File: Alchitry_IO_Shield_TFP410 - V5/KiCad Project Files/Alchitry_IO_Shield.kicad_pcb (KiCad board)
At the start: 2 copper layers, 65 x 45 mm, 75 parts, among them J0 HDMI_A_1.4, Q1 Q_PMOS_SGD, Q2 Q_PMOS_SGD, Q3 Q_PMOS_SGD, Q4 Q_PMOS_SGD, SW1 SW_DIP_x08, SW2 SW_DIP_x08, SW3 SW_DIP_x08, U0 boardmezzanine_new, U1 TFP410

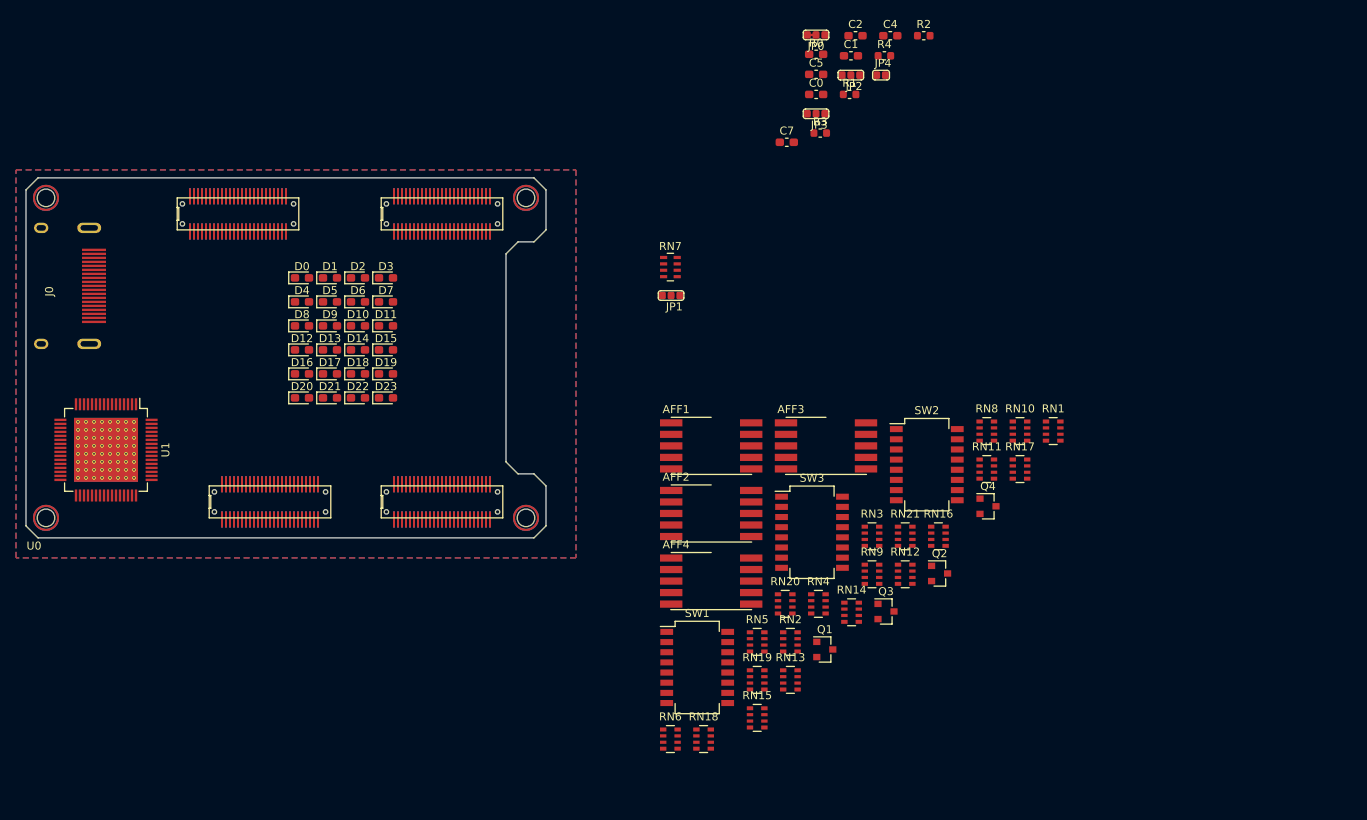
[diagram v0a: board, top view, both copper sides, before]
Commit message: grouped footprints by function
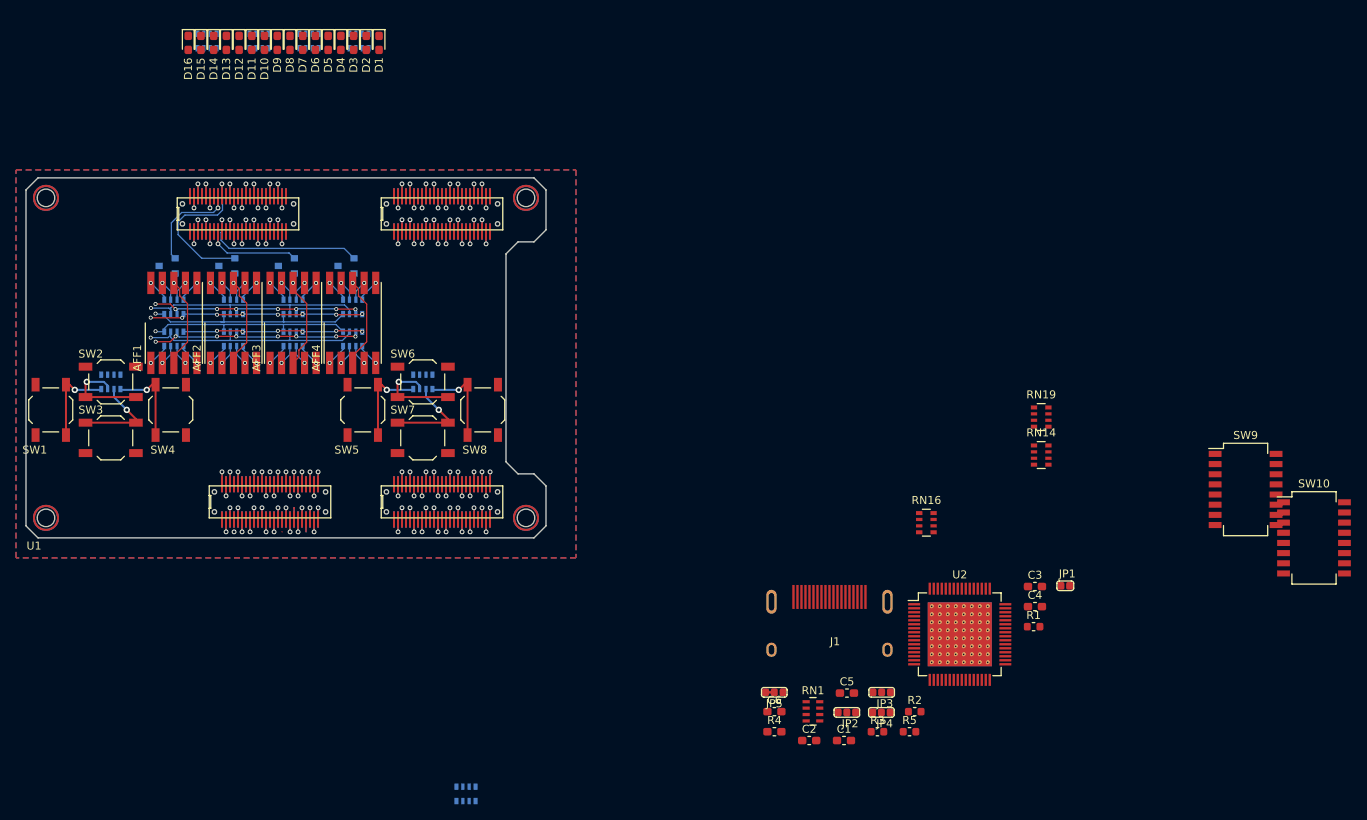
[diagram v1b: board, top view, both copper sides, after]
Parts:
- removed C0, C7: 100nF, Capacitor_SMD:C_0603_1608Metric_Pad1.05x0.95mm_HandSolder
- removed D0, D17, D18, D19, D20, D21, D22, D23: LED, LED_SMD:LED_0603_1608Metric_Pad1.05x0.95mm_HandSolder
- removed J0: HDMI_A_1.4, Custom_Parts:HDMI
- removed JP0: V_Sel, Custom_Parts:jumper_1_2_bridged
- removed R0: 510, Resistor_SMD:R_0603_1608Metric_Pad1.05x0.95mm_HandSolder
- removed RN20, RN21: R_Pack04, Resistor_SMD:R_Array_Convex_4x0603
- removed the U1 at (22.0, 46.0)
- added C3: 100nF, Capacitor_SMD:C_0603_1608Metric_Pad1.05x0.95mm_HandSolder, F.Cu at (138.1, 63.1)
- added C6: 100nF, Capacitor_SMD:C_0603_1608Metric_Pad1.05x0.95mm_HandSolder, F.Cu at (105.5, 78.7)
- added J1: HDMI_A_1.4, Custom_Parts:HDMI, F.Cu at (116.9, 64.4)
- added JP5: V_Sel, Custom_Parts:jumper_1_2_bridged, F.Cu at (105.5, 76.3)
- added R5: 10K, Resistor_SMD:R_0603_1608Metric, F.Cu at (122.4, 81.2)
- added SW10: SW_DIP_x08, Button_Switch_SMD:SW_DIP_SPSTx08_Slide_Copal_CHS-08B_W7.62mm_P1.27mm, F.Cu at (173.0, 57.0)
- added SW4: SWL4, Button_Switch_SMD:SW_SPST_TL3342, F.Cu at (30.1, 41.0)
- added SW5: SWR3, Button_Switch_SMD:SW_SPST_TL3342, F.Cu at (54.1, 41.0)
- added SW6: SWR1, Button_Switch_SMD:SW_SPST_TL3342, F.Cu at (61.6, 37.5)
- added SW7: SWR2, Button_Switch_SMD:SW_SPST_TL3342, F.Cu at (61.6, 44.5)
- added SW8: SWR3, Button_Switch_SMD:SW_SPST_TL3342, F.Cu at (69.1, 41.0)
- added SW9: SW_DIP_x08, Button_Switch_SMD:SW_DIP_SPSTx08_Slide_Copal_CHS-08B_W7.62mm_P1.27mm, F.Cu at (164.4, 51.0)
- added U2: TFP410, Package_QFP:HTQFP-64-1EP_10x10mm_P0.5mm_EP8x8mm_Mask4.4x4.4mm_ThermalVias, F.Cu at (128.7, 69.0)
- AFF1, AFF2, AFF3, AFF4: footprint Display_7Segment:KCSC02-136 -> Display_7Segment:KCSC02-105
- JP1: value DK1 -> DKEN; footprint Custom_Parts:jumper_unbridged -> Custom_Parts:Jumper_2_Pin_Unbridged
- JP3: value DK3 -> DK1
- JP4: value DKEN -> DK3; footprint Custom_Parts:Jumper_2_Pin_Unbridged -> Custom_Parts:jumper_unbridged
- Q1, Q2, Q3, Q4, RN10, RN11, RN12, RN13, RN15, RN17, RN18, RN2, RN3, RN4, RN5, RN6, RN8, RN9: moved to B.Cu
- R1: value 10K -> 33K
- R2: value 10K -> 91K
- R3: value 33K -> 10K
- R4: value 91K -> 510; footprint Resistor_SMD:R_0603_1608Metric -> Resistor_SMD:R_0603_1608Metric_Pad1.05x0.95mm_HandSolder
- RN1: value R_Pack04 -> 10K; footprint Resistor_SMD:R_Array_Convex_4x0603 -> Resistor_SMD:R_Array_Concave_4x0603
- RN7: value 10K -> R_Pack04; footprint Resistor_SMD:R_Array_Concave_4x0603 -> Resistor_SMD:R_Array_Convex_4x0603; moved to B.Cu
- SW1: value SW_DIP_x08 -> SWL3; footprint Button_Switch_SMD:SW_DIP_SPSTx08_Slide_Copal_CHS-08B_W7.62mm_P1.27mm -> Button_Switch_SMD:SW_SPST_TL3342
- SW2: value SW_DIP_x08 -> SWL1; footprint Button_Switch_SMD:SW_DIP_SPSTx08_Slide_Copal_CHS-08B_W7.62mm_P1.27mm -> Button_Switch_SMD:SW_SPST_TL3342
- SW3: value SW_DIP_x08 -> SWL2; footprint Button_Switch_SMD:SW_DIP_SPSTx08_Slide_Copal_CHS-08B_W7.62mm_P1.27mm -> Button_Switch_SMD:SW_SPST_TL3342
- moved RN15 109.0 mm to (34.6, -5.11), turned to 90 degrees
- moved RN12 104.7 mm to (41.1, -5.11), turned to 90 degrees
- moved SW2 102.5 mm to (22.6, 37.5), turned to 180 degrees
- moved Q2 97.0 mm to (37.1, 23.0), turned to 180 degrees
- moved RN9 96.9 mm to (47.4, -5.11), turned to 90 degrees
- moved Q1 95.2 mm to (29.6, 23.0), turned to 180 degrees
- moved RN4 92.7 mm to (22.6, 37.5), turned to 90 degrees
- moved RN3 91.9 mm to (30.5, 28.1), turned to 90 degrees
- moved RN10 91.6 mm to (45.4, 32.1), turned to -90 degrees
- moved RN5 90.1 mm to (53.6, -5.11), turned to 90 degrees
- moved RN11 89.1 mm to (45.4, 28.1), turned to 90 degrees
- moved SW3 88.4 mm to (22.6, 44.5)
- moved C2 88.3 mm to (109.9, 82.3)
- moved SW1 87.0 mm to (15.1, 41.0), turned to -90 degrees
- moved Q3 86.5 mm to (44.5, 23.0), turned to 180 degrees
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- renumbered U0 to U1
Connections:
- net /LED17 renamed Net-(U1-PadAB_20)
- net /LED18 renamed Net-(U1-PadAB_18)
- net /LED19 renamed Net-(U1-PadAB_17)
- net /LED20 renamed Net-(U1-PadAB_15)
- net /LED21 renamed Net-(U1-PadAB_14)
- net /LED22 renamed Net-(U1-PadAB_12)
- net /LED23 renamed Net-(U1-PadAB_11)
- D1 pad 2: /LED1 -> /LED0
- D10 pad 2: /LED10 -> /LED9
- D11 pad 2: /LED11 -> /LED10
- D12 pad 2: /LED12 -> /LED11
- D13 pad 2: /LED13 -> /LED12
- D14 pad 2: /LED14 -> /LED13
- D15 pad 2: /LED15 -> /LED14
- D16 pad 2: /LED16 -> /LED15
- D2 pad 2: /LED2 -> /LED1
- D3 pad 2: /LED3 -> /LED2
- D4 pad 2: /LED4 -> /LED3
- D5 pad 2: /LED5 -> /LED4
- D6 pad 2: /LED6 -> /LED5
- D7 pad 2: /LED7 -> /LED6
- D8 pad 2: /LED8 -> /LED7
- D9 pad 2: /LED9 -> /LED8
- JP1 pad 1: +3V3 -> GNDREF
- JP1 pad 2: /HDMI/DK1 -> Net-(JP1-Pad2)
- JP3 pad 2: /HDMI/DK3 -> /HDMI/DK1
- JP4 pad 1: GNDREF -> +3V3
- JP4 pad 2: Net-(JP4-Pad2) -> /HDMI/DK3
- R1 pad 1: /HDMI/ISEL -> Net-(R1-Pad1)
- R1 pad 2: GNDREF -> +3V3
- R2 pad 1: Net-(R2-Pad1) -> Net-(R1-Pad1)
- R3 pad 2: +3V3 -> GNDREF
- R4 pad 1: Net-(R3-Pad1) -> +3V3
- R4 pad 2: GNDREF -> Net-(R4-Pad2)
- RN1 pad 1: GNDREF -> +3V3
- RN1 pad 2: GNDREF -> +3V3
- RN1 pad 3: GNDREF -> +3V3
- RN1 pad 4: GNDREF -> +3V3
- RN1 pad 5: Net-(D3-Pad1) -> Net-(RN1-Pad5)
- RN1 pad 6: Net-(D2-Pad1) -> Net-(RN1-Pad6)
- RN1 pad 7: Net-(D1-Pad1) -> Net-(JP1-Pad2)
- RN10 pad 1: +3V3 -> /C4
- RN10 pad 2: +3V3 -> /C3
- RN10 pad 3: +3V3 -> /C2
- RN10 pad 4: +3V3 -> /DP
- RN10 pad 5: Net-(RN10-Pad5) -> Net-(AFF3-Pad5)
- RN10 pad 6: Net-(RN10-Pad6) -> Net-(AFF3-Pad4)
- RN10 pad 7: Net-(RN10-Pad7) -> Net-(AFF3-Pad2)
- RN10 pad 8: Net-(RN10-Pad8) -> Net-(AFF3-Pad1)
- RN11 pad 1: +3V3 -> /C1
- RN11 pad 2: +3V3 -> /C0
- RN11 pad 3: +3V3 -> /C5
- RN11 pad 4: +3V3 -> /C6
- RN11 pad 5: Net-(RN11-Pad5) -> Net-(AFF3-Pad10)
- RN11 pad 6: Net-(RN11-Pad6) -> Net-(AFF3-Pad9)
- RN11 pad 7: Net-(RN11-Pad7) -> Net-(AFF3-Pad7)
- RN11 pad 8: Net-(RN11-Pad8) -> Net-(AFF3-Pad6)
- RN12 pad 1: +3V3 -> GNDREF
- RN12 pad 2: +3V3 -> GNDREF
- RN12 pad 3: +3V3 -> GNDREF
- RN12 pad 4: +3V3 -> GNDREF
- RN12 pad 5: Net-(RN12-Pad5) -> Net-(D12-Pad1)
- RN12 pad 6: Net-(RN12-Pad6) -> Net-(D11-Pad1)
- RN12 pad 7: Net-(RN12-Pad7) -> Net-(D10-Pad1)
- RN12 pad 8: Net-(RN12-Pad8) -> Net-(D9-Pad1)
- RN13 pad 1: +3V3 -> GNDREF
- RN13 pad 2: +3V3 -> GNDREF
- RN13 pad 3: +3V3 -> GNDREF
- RN13 pad 4: +3V3 -> GNDREF
- RN13 pad 5: Net-(RN13-Pad5) -> /DIP3
- RN13 pad 6: Net-(RN13-Pad6) -> /DIP2
- RN13 pad 7: Net-(RN13-Pad7) -> /DIP1
- RN13 pad 8: Net-(RN13-Pad8) -> /DIP0
- RN14 pad 1: /C0 -> GNDREF
- RN14 pad 2: /C1 -> GNDREF
- RN14 pad 3: /C2 -> GNDREF
- RN14 pad 4: /C3 -> GNDREF
- RN14 pad 5: Net-(AFF1-Pad2) -> /DIP7
- RN14 pad 6: Net-(AFF1-Pad4) -> /DIP6
- RN14 pad 7: Net-(AFF1-Pad6) -> /DIP5
- RN14 pad 8: Net-(AFF1-Pad7) -> /DIP4
- RN15 pad 1: /C0 -> GNDREF
- RN15 pad 2: /C1 -> GNDREF
- RN15 pad 3: /C2 -> GNDREF
- RN15 pad 4: /C3 -> GNDREF
- RN15 pad 5: Net-(AFF2-Pad2) -> Net-(D16-Pad1)
- RN15 pad 6: Net-(AFF2-Pad4) -> Net-(D15-Pad1)
- RN15 pad 7: Net-(AFF2-Pad6) -> Net-(D14-Pad1)
- RN15 pad 8: Net-(AFF2-Pad7) -> Net-(D13-Pad1)
- RN16 pad 1: /C4 -> GNDREF
- RN16 pad 2: /C5 -> GNDREF
- RN16 pad 3: /C6 -> GNDREF
- RN16 pad 4: /DP -> GNDREF
- RN16 pad 5: Net-(AFF1-Pad5) -> /DIP11
- RN16 pad 6: Net-(AFF1-Pad10) -> /DIP10
- RN16 pad 7: Net-(AFF1-Pad9) -> /DIP9
- RN16 pad 8: Net-(AFF1-Pad1) -> /DIP8
- RN17 pad 2: /C5 -> /C3
- RN17 pad 3: /C6 -> /C2
- RN17 pad 5: Net-(AFF2-Pad5) -> Net-(AFF4-Pad5)
- RN17 pad 6: Net-(AFF2-Pad10) -> Net-(AFF4-Pad4)
- RN17 pad 7: Net-(AFF2-Pad9) -> Net-(AFF4-Pad2)
- RN17 pad 8: Net-(AFF2-Pad1) -> Net-(AFF4-Pad1)
- RN18 pad 1: /C0 -> /C1
- RN18 pad 2: /C1 -> /C0
- RN18 pad 3: /C2 -> /C5
- RN18 pad 4: /C3 -> /C6
- RN18 pad 5: Net-(AFF3-Pad2) -> Net-(AFF4-Pad10)
- RN18 pad 6: Net-(AFF3-Pad4) -> Net-(AFF4-Pad9)
- RN18 pad 7: Net-(AFF3-Pad6) -> Net-(AFF4-Pad7)
- RN18 pad 8: Net-(AFF3-Pad7) -> Net-(AFF4-Pad6)
- RN19 pad 1: /C0 -> GNDREF
- RN19 pad 2: /C1 -> GNDREF
- RN19 pad 3: /C2 -> GNDREF
- RN19 pad 4: /C3 -> GNDREF
- RN19 pad 5: Net-(AFF4-Pad2) -> /DIP15
- RN19 pad 6: Net-(AFF4-Pad4) -> /DIP14
- RN19 pad 7: Net-(AFF4-Pad6) -> /DIP13
- RN19 pad 8: Net-(AFF4-Pad7) -> /DIP12
- RN2 pad 1: GNDREF -> /C4
- RN2 pad 2: GNDREF -> /C3
- RN2 pad 3: GNDREF -> /C2
- RN2 pad 4: GNDREF -> /DP
- RN2 pad 5: Net-(D7-Pad1) -> Net-(AFF1-Pad5)
- RN2 pad 6: Net-(D6-Pad1) -> Net-(AFF1-Pad4)
- RN2 pad 7: Net-(D5-Pad1) -> Net-(AFF1-Pad2)
- RN2 pad 8: Net-(D4-Pad1) -> Net-(AFF1-Pad1)
- RN3 pad 1: GNDREF -> /C1
- RN3 pad 2: GNDREF -> /C0
- RN3 pad 3: GNDREF -> /C5
- RN3 pad 4: GNDREF -> /C6
- RN3 pad 5: Net-(D11-Pad1) -> Net-(AFF1-Pad10)
- RN3 pad 6: Net-(D10-Pad1) -> Net-(AFF1-Pad9)
- RN3 pad 7: Net-(D9-Pad1) -> Net-(AFF1-Pad7)
- RN3 pad 8: Net-(D8-Pad1) -> Net-(AFF1-Pad6)
- RN4 pad 1: GNDREF -> /SWL4
- RN4 pad 2: GNDREF -> /SWL2
- RN4 pad 3: GNDREF -> /SWL1
- RN4 pad 4: GNDREF -> /SWL3
- RN4 pad 5: Net-(D15-Pad1) -> GNDREF
- RN4 pad 6: Net-(D14-Pad1) -> GNDREF
- RN4 pad 7: Net-(D13-Pad1) -> GNDREF
- RN4 pad 8: Net-(D12-Pad1) -> GNDREF
- RN5 pad 5: Net-(D19-Pad1) -> Net-(D4-Pad1)
- RN5 pad 6: Net-(D18-Pad1) -> Net-(D3-Pad1)
- RN5 pad 7: Net-(D17-Pad1) -> Net-(D2-Pad1)
- RN5 pad 8: Net-(D16-Pad1) -> Net-(D1-Pad1)
- RN6 pad 1: GNDREF -> /C4
- RN6 pad 2: GNDREF -> /C3
- RN6 pad 3: GNDREF -> /C2
- RN6 pad 4: GNDREF -> /DP
- RN6 pad 5: Net-(D23-Pad1) -> Net-(AFF2-Pad5)
- RN6 pad 6: Net-(D22-Pad1) -> Net-(AFF2-Pad4)
- RN6 pad 7: Net-(D21-Pad1) -> Net-(AFF2-Pad2)
- RN6 pad 8: Net-(D20-Pad1) -> Net-(AFF2-Pad1)
- RN7 pad 1: +3V3 -> /C1
- RN7 pad 2: +3V3 -> /C0
- RN7 pad 3: +3V3 -> /C5
- RN7 pad 4: +3V3 -> /C6
- RN7 pad 5: Net-(RN7-Pad5) -> Net-(AFF2-Pad10)
- RN7 pad 6: Net-(RN7-Pad6) -> Net-(AFF2-Pad9)
- RN7 pad 7: Net-(JP4-Pad2) -> Net-(AFF2-Pad7)
- RN7 pad 8: Net-(RN7-Pad8) -> Net-(AFF2-Pad6)
- RN8 pad 1: +3V3 -> /SWR4
- RN8 pad 2: +3V3 -> /SWR2
- RN8 pad 3: +3V3 -> /SWR1
- RN8 pad 4: +3V3 -> /SWR3
- RN8 pad 5: Net-(RN8-Pad5) -> GNDREF
- RN8 pad 6: Net-(RN8-Pad6) -> GNDREF
- RN8 pad 7: Net-(RN8-Pad7) -> GNDREF
- RN8 pad 8: Net-(RN8-Pad8) -> GNDREF
- RN9 pad 1: +3V3 -> GNDREF
- RN9 pad 2: +3V3 -> GNDREF
- RN9 pad 3: +3V3 -> GNDREF
- RN9 pad 4: +3V3 -> GNDREF
- RN9 pad 5: Net-(RN9-Pad5) -> Net-(D8-Pad1)
- RN9 pad 6: Net-(RN9-Pad6) -> Net-(D7-Pad1)
- RN9 pad 7: Net-(RN9-Pad7) -> Net-(D6-Pad1)
- RN9 pad 8: Net-(RN9-Pad8) -> Net-(D5-Pad1)
- SW1 pad 1: /DIP7 -> /SWL3
- SW1 pad 2: /DIP6 -> +3V3
- SW2 pad 1: /DIP15 -> /SWL1
- SW2 pad 2: /DIP14 -> +3V3
- SW3 pad 1: /DIP23 -> /SWL2
- SW3 pad 2: /DIP22 -> +3V3
- U1 pad AB_21: /LED16 -> Net-(U1-PadAB_21)
- U1 pad AB_30: /DIP16 -> Net-(U1-PadAB_30)
- U1 pad AB_31: /DIP17 -> Net-(U1-PadAB_31)
- U1 pad AB_33: /DIP18 -> Net-(U1-PadAB_33)
- U1 pad AB_34: /DIP19 -> Net-(U1-PadAB_34)
- U1 pad AB_36: /DIP20 -> Net-(U1-PadAB_36)
- U1 pad AB_37: /DIP21 -> Net-(U1-PadAB_37)
- U1 pad AB_39: /DIP22 -> Net-(U1-PadAB_39)
- U1 pad AB_40: /DIP23 -> Net-(U1-PadAB_40)
- U1 pad AT_21: /LED16 -> Net-(U1-PadAB_21)
- U1 pad AT_30: /DIP16 -> Net-(U1-PadAB_30)
- U1 pad AT_31: /DIP17 -> Net-(U1-PadAB_31)
- U1 pad AT_33: /DIP18 -> Net-(U1-PadAB_33)
- U1 pad AT_34: /DIP19 -> Net-(U1-PadAB_34)
- U1 pad AT_36: /DIP20 -> Net-(U1-PadAB_36)
- U1 pad AT_37: /DIP21 -> Net-(U1-PadAB_37)
- U1 pad AT_39: /DIP22 -> Net-(U1-PadAB_39)
- U1 pad AT_40: /DIP23 -> Net-(U1-PadAB_40)
- U1 pad BB_1: Net-(U0-PadBB_1) -> +5V
- U1 pad BB_23: /BTN2 -> /SWL3
- U1 pad BB_24: /BTN3 -> /SWL4
- U1 pad BB_27: /BTN1 -> /SWL2
- U1 pad BB_28: /BTN0 -> /SWL1
- U1 pad BB_50: Net-(U0-PadBB_50) -> +5V
- U1 pad BT_1: Net-(U0-PadBB_1) -> +5V
- U1 pad BT_23: /BTN2 -> /SWL3
- U1 pad BT_24: /BTN3 -> /SWL4
- U1 pad BT_27: /BTN1 -> /SWL2
- U1 pad BT_28: /BTN0 -> /SWL1
- U1 pad BT_50: Net-(U0-PadBB_50) -> +5V
- U1 pad CB_1: Net-(U0-PadCB_1) -> +5V
- U1 pad CB_45: Net-(U0-PadCB_45) -> /SWR4
- U1 pad CB_46: /BTN6 -> /SWR3
- U1 pad CB_48: /BTN5 -> /SWR2
- U1 pad CB_49: /BTN4 -> /SWR1
- U1 pad CB_50: Net-(U0-PadCB_50) -> +5V
- U1 pad CT_1: Net-(U0-PadCB_1) -> +5V
- U1 pad CT_45: Net-(U0-PadCB_45) -> /SWR4
- U1 pad CT_46: /BTN6 -> /SWR3
- U1 pad CT_48: /BTN5 -> /SWR2
- U1 pad CT_49: /BTN4 -> /SWR1
- U1 pad CT_50: Net-(U0-PadCB_50) -> +5V
- U1 pad DB_1: Net-(U0-PadDB_1) -> +5V
- U1 pad DB_50: Net-(U0-PadDB_50) -> +5V
- U1 pad DT_1: Net-(U0-PadDB_1) -> +5V
- U1 pad DT_50: Net-(U0-PadDB_50) -> +5V
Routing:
- net /C5: track 0.00 -> 32.5 mm, vias 0 -> 2
- net /C3: track 0.00 -> 32.2 mm, vias 0 -> 2
- net /C0: track 0.00 -> 31.2 mm, vias 0 -> 9
- net /C2: track 0.00 -> 31.1 mm, vias 0 -> 9
- net /C1: track 0.00 -> 29.9 mm, vias 0 -> 9
- net /C6: track 0.00 -> 29.7 mm, vias 0 -> 2
- net /C4: track 0.00 -> 29.2 mm, vias 0 -> 2
- net /DP: track 0.00 -> 25.6 mm, vias 0 -> 7
- net /AN3: track 0.00 -> 21.6 mm, vias 0 -> 1
- net /AN1: track 0.00 -> 20.8 mm, vias 0 -> 1
- net /SWL2: track 0.00 -> 14.6 mm, vias 0 -> 2
- net /SWR2: track 0.00 -> 14.6 mm, vias 0 -> 2
- net /SWL1: track 0.00 -> 14.4 mm, vias 0 -> 2
- net /SWR1: track 0.00 -> 14.4 mm, vias 0 -> 2
- net /AN0: track 0.00 -> 14.2 mm, vias 0 -> 1
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
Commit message: minor changes
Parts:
- moved RN8 39.2 mm to (22.4, 37.6)
- moved SW5 39.2 mm to (14.9, 41.1)
- moved SW6 39.2 mm to (22.4, 37.6)
- moved SW7 39.2 mm to (22.4, 44.6)
- moved SW8 39.2 mm to (29.9, 41.1)
- moved SW4 38.5 mm to (68.6, 41.1)
- moved RN4 38.5 mm to (61.1, 37.6)
- moved SW1 38.5 mm to (53.6, 41.1)
- moved SW2 38.5 mm to (61.1, 37.6)
- moved SW3 38.5 mm to (61.1, 44.6)
- moved D1 33.2 mm to (70.2, 25.2)
- moved D2 33.2 mm to (68.6, 25.2)
- moved D6 33.2 mm to (62.2, 25.2)
- moved D8 33.2 mm to (59.0, 25.2)
- moved RN5 33.2 mm to (67.7, 25.0)
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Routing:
- net /SWL1: track 14.4 -> 60.1 mm
- net /SWL2: track 14.6 -> 56.2 mm
- net /SWL3: track 13.9 -> 48.1 mm
- net +3V3: track 8.96 -> 42.8 mm
- net /SWR3: track 13.9 -> 37.1 mm, vias 2 -> 3
- net /SWL4: track 13.9 -> 34.9 mm
- net /AN3: track 21.6 -> 2.66 mm
- net /SWR1: track 14.4 -> 33.3 mm
- net /AN1: track 20.8 -> 2.66 mm
- net /SWR2: track 14.6 -> 29.7 mm, vias 2 -> 3
- net /SWR4: track 13.9 -> 28.9 mm
- net /AN0: track 14.2 -> 2.66 mm
- net /AN2: track 13.2 -> 2.66 mm
- net /LED7: track 2.93 -> 12.1 mm
- net /LED0: track 2.93 -> 11.6 mm
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
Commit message: started new shield
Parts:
- removed AFF1, AFF2, AFF3, AFF4: LTS-6960HR, Display_7Segment:KCSC02-105
- removed RN10, RN11, RN13, RN14, RN16, RN17, RN18, RN19, RN2, RN3, RN6, RN7: R_Pack04, Resistor_SMD:R_Array_Convex_4x0603
- removed SW10, SW9: SW_DIP_x08, Button_Switch_SMD:SW_DIP_SPSTx08_Slide_Copal_CHS-08B_W7.62mm_P1.27mm
- added U3: 0402_7Seg_CA, Custom_LEDs:0402_7Seg_CA_W_Res, F.Cu at (18.0, 32.0)
- added U4: 0402_7Seg_CA, Custom_LEDs:0402_7Seg_CA_W_Res, F.Cu at (22.0, 32.0)
- added U5: 0402_7Seg_CA, Custom_LEDs:0402_7Seg_CA_W_Res, F.Cu at (62.0, 32.0)
- added U6: 0402_7Seg_CA, Custom_LEDs:0402_7Seg_CA_W_Res, F.Cu at (66.0, 32.0)
- D1, D10, D11, D12, D13, D14, D15, D16, D2, D3, D4, D5, D6, D7, D8, D9: footprint LED_SMD:LED_0603_1608Metric_Pad1.05x0.95mm_HandSolder -> LED_SMD:LED_0402_1005Metric
- Q1, Q2, Q3, Q4, RN4, RN8: moved to F.Cu
- SW1, SW2, SW3, SW4, SW5, SW6, SW7, SW8: footprint Button_Switch_SMD:SW_SPST_TL3342 -> Custom_Buttons:Korean Hroparts Elec K2-1177SR
- U1: value boardmezzanine_new -> Alchitry_Single; footprint Custom_Parts:Alchitry_Top_Bottom -> Alchitry_Footprints:Alchitry_Bottom
- moved Q1 72.0 mm to (99.0, 42.7)
- moved Q2 69.2 mm to (105.0, 36.1)
- moved C1 68.2 mm to (105.6, 14.7)
- moved R5 67.1 mm to (114.1, 14.7)
- moved C2 63.5 mm to (100.7, 19.5)
- moved JP5 61.9 mm to (100.7, 14.6)
- moved C5 61.9 mm to (109.9, 14.7)
- moved C4 61.3 mm to (100.7, 17.0)
- moved R3 60.7 mm to (104.8, 22.0)
- moved JP2 60.0 mm to (105.0, 19.6)
- moved R4 59.4 mm to (100.7, 22.0)
- moved R1 58.5 mm to (109.2, 17.2)
- moved Q3 58.0 mm to (100.5, 38.1)
- moved Q4 57.7 mm to (109.0, 31.6)
- moved JP4 57.4 mm to (100.7, 24.4)
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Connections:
- J1 pad 13: Net-(J1-Pad13) -> (no net)
- J1 pad 14: Net-(J1-Pad14) -> (no net)
- J1 pad 15: Net-(J1-Pad15) -> (no net)
- J1 pad 16: Net-(J1-Pad16) -> (no net)
- J1 pad 19: Net-(J1-Pad19) -> (no net)
- Q2 pad 1: /AN1 -> +3V3
- RN4 pad 1: /SWL4 -> /SWL1
- RN4 pad 2: /SWL2 -> /SWL3
- RN4 pad 3: /SWL1 -> /SWL2
- RN4 pad 4: /SWL3 -> /SWL4
- RN8 pad 1: /SWR4 -> /SWR1
- RN8 pad 2: /SWR2 -> /SWR3
- RN8 pad 3: /SWR1 -> /SWR2
- RN8 pad 4: /SWR3 -> /SWR4
- U2 pad 11: Net-(U2-Pad11) -> (no net)
- U2 pad 49: Net-(U2-Pad49) -> (no net)
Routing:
- net /SWL1: track 60.1 -> 0.00 mm, vias 2 -> 0
- net /SWL2: track 56.2 -> 0.00 mm, vias 2 -> 0
- net /SWL3: track 48.1 -> 0.00 mm, vias 2 -> 0
- net +3V3: track 42.8 -> 0.00 mm, vias 3 -> 0
- net /SWR3: track 37.1 -> 0.00 mm, vias 3 -> 0
- net /SWL4: track 34.9 -> 0.00 mm, vias 2 -> 0
- net /SWR1: track 33.3 -> 0.00 mm, vias 2 -> 0
- net /C5: track 32.2 -> 0.00 mm, vias 2 -> 0
- net /C3: track 31.9 -> 0.00 mm, vias 2 -> 0
- net /C0: track 31.0 -> 0.00 mm, vias 9 -> 0
- net /C2: track 30.9 -> 0.00 mm, vias 9 -> 0
- net /SWR2: track 29.7 -> 0.00 mm, vias 3 -> 0
- net /C1: track 29.7 -> 0.00 mm, vias 9 -> 0
- net /C6: track 29.4 -> 0.00 mm, vias 2 -> 0
- net /C4: track 29.0 -> 0.00 mm, vias 2 -> 0
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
